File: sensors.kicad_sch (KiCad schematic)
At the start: 9 parts, among them IC7 BME690, U2 BME280, U3 BMP581

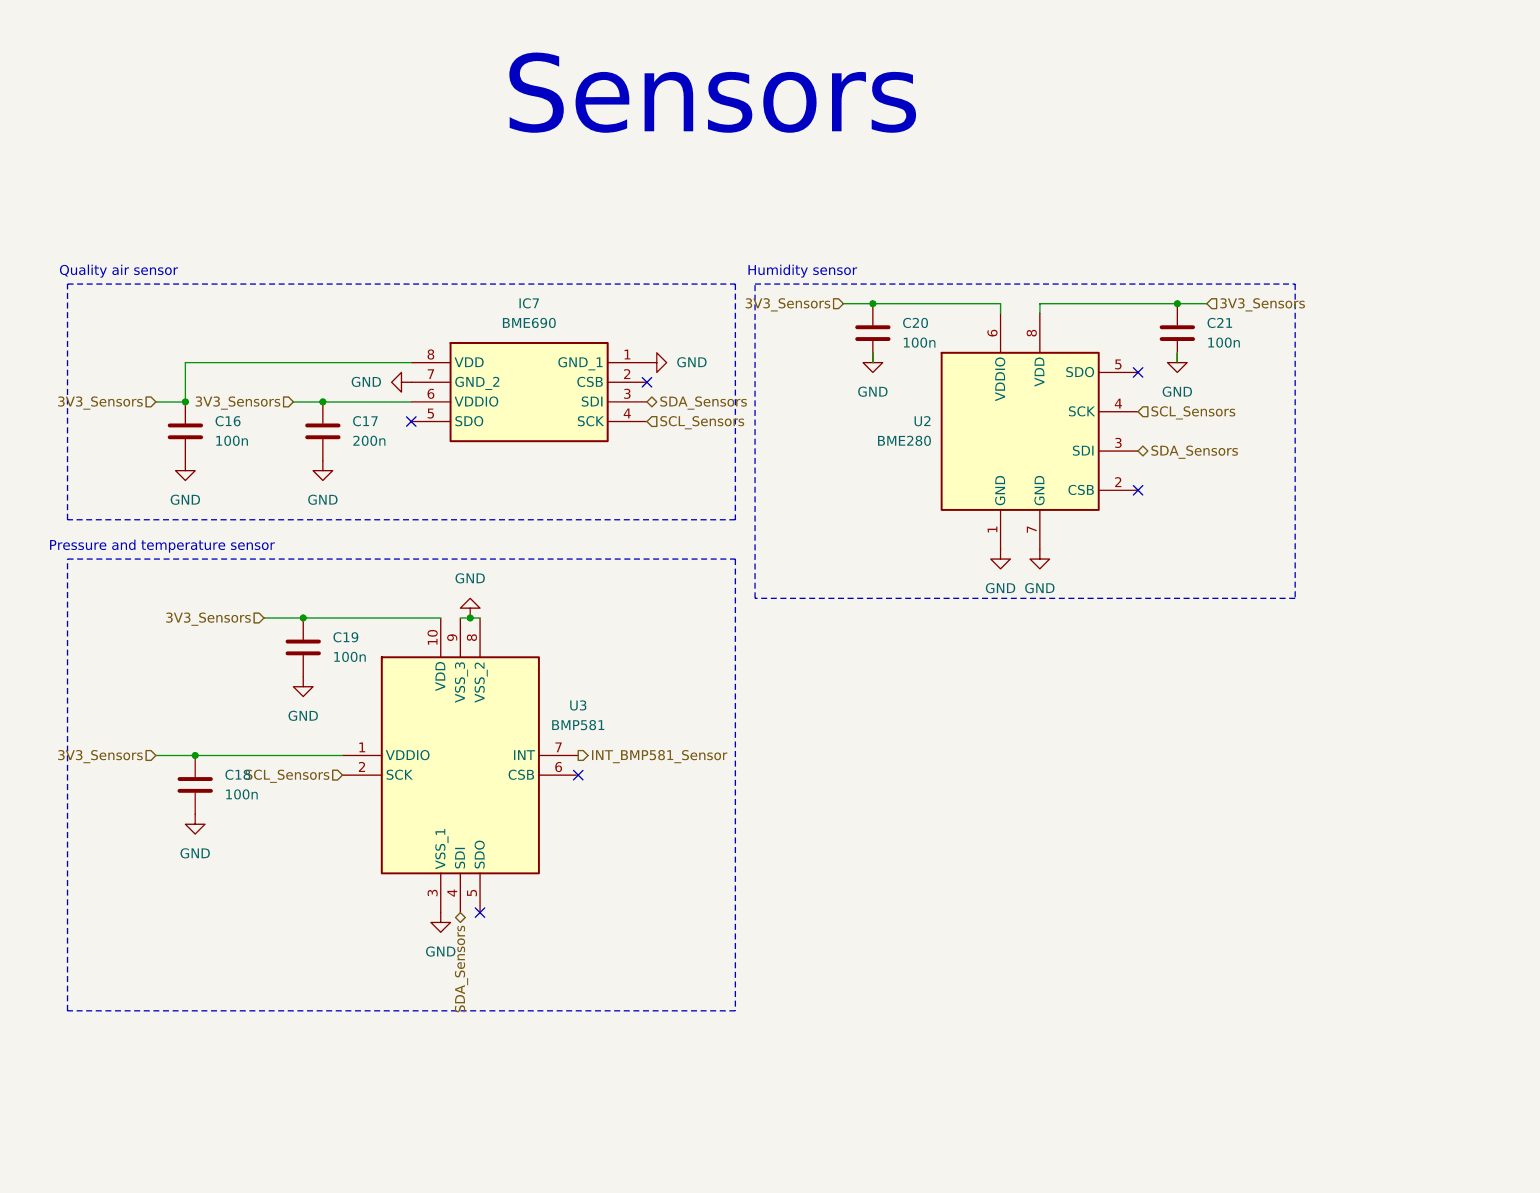
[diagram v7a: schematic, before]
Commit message: Fix some little warnings and refomat schematics files
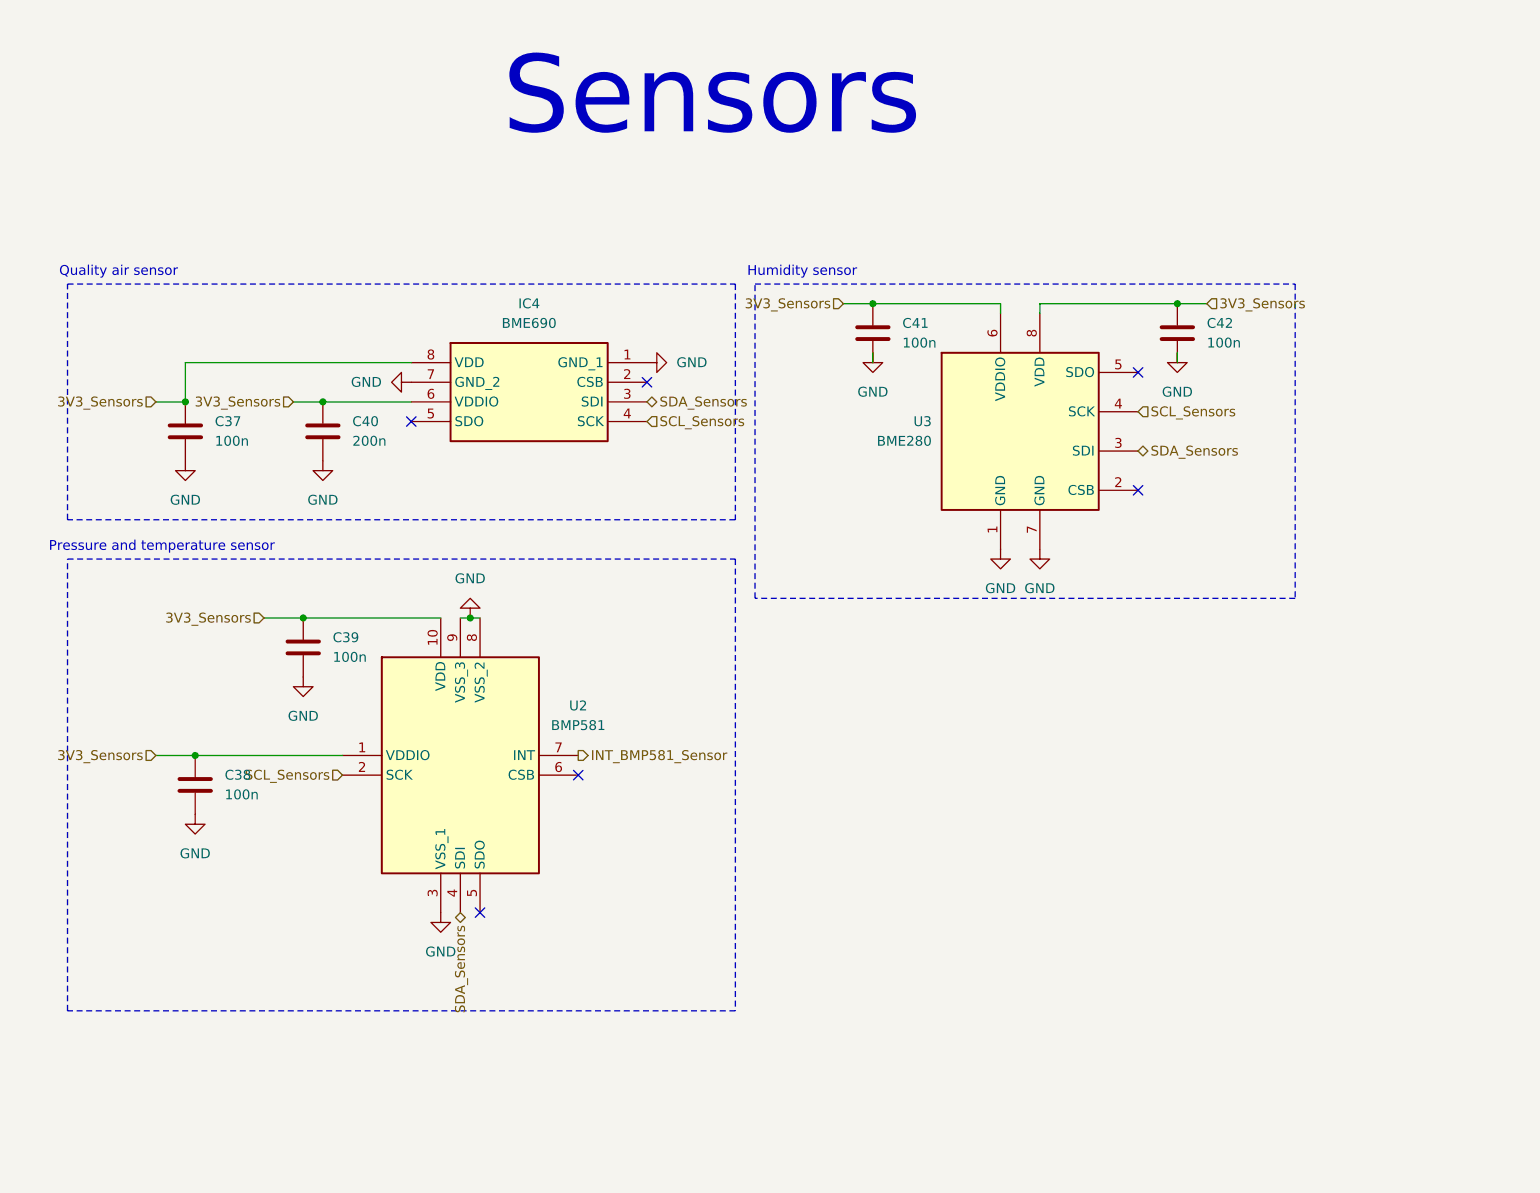
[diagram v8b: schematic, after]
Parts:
- renumbered C16 to C37, C18 to C38, C19 to C39, C17 to C40, C20 to C41, C21 to C42, IC7 to IC4, U3 to U2, U2 to U3
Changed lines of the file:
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@@
 		(dnp no)
 		(fields_autoplaced yes)
-		(property "Reference" "#PWR046"
+		(property "Reference" "#PWR070"
 			(at 170.18 66.04 0)
 			(effects
@@
 			(project "weather-station-poc"
 				(path "/38eb53bb-294e-46e4-ad59-fd355ca373b9/29574217-d56b-4a63-a2c4-128dfec2758e"
-					(reference "#PWR046")
+					(reference "#PWR070")
 					(unit 1)
 				)
@@
 		(dnp no)
 		(fields_autoplaced yes)
-		(property "Reference" "#PWR039"
+		(property "Reference" "#PWR069"
 			(at 147.32 60.96 0)
 			(effects
@@
 			(project "weather-station-poc"
 				(path "/38eb53bb-294e-46e4-ad59-fd355ca373b9/29574217-d56b-4a63-a2c4-128dfec2758e"
-					(reference "#PWR039")
+					(reference "#PWR069")
 					(unit 1)
 				)
@@
 		(dnp no)
 		(fields_autoplaced yes)
-		(property "Reference" "C21"
+		(property "Reference" "C42"
 			(at 213.36 55.8799 0)
 			(effects
@@
 			(project "weather-station-poc"
 				(path "/38eb53bb-294e-46e4-ad59-fd355ca373b9/29574217-d56b-4a63-a2c4-128dfec2758e"
-					(reference "C21")
+					(reference "C42")
 					(unit 1)
 				)
@@
 		(dnp no)
 		(fields_autoplaced yes)
-		(property "Reference" "C16"
+		(property "Reference" "C37"
 			(at 85.09 68.5799 0)
 			(effects
@@
 			(project ""
 				(path "/38eb53bb-294e-46e4-ad59-fd355ca373b9/29574217-d56b-4a63-a2c4-128dfec2758e"
-					(reference "C16")
+					(reference "C37")
 					(unit 1)
 				)
@@
 		(dnp no)
 		(fields_autoplaced yes)
-		(property "Reference" "#PWR036"
+		(property "Reference" "#PWR062"
 			(at 81.28 80.01 0)
 			(effects
@@
 			(project ""
 				(path "/38eb53bb-294e-46e4-ad59-fd355ca373b9/29574217-d56b-4a63-a2c4-128dfec2758e"
-					(reference "#PWR036")
+					(reference "#PWR062")
 					(unit 1)
 				)
@@
 		(dnp no)
 		(fields_autoplaced yes)
-		(property "Reference" "#PWR048"
+		(property "Reference" "#PWR072"
 			(at 191.77 91.44 0)
 			(effects
@@
 			(project "weather-station-poc"
 				(path "/38eb53bb-294e-46e4-ad59-fd355ca373b9/29574217-d56b-4a63-a2c4-128dfec2758e"
-					(reference "#PWR048")
+					(reference "#PWR072")
 					(unit 1)
 				)
@@
 		(dnp no)
 		(fields_autoplaced yes)
-		(property "Reference" "#PWR042"
+		(property "Reference" "#PWR068"
 			(at 118.11 87.63 0)
 			(effects
@@
 			(project "weather-station-poc"
 				(path "/38eb53bb-294e-46e4-ad59-fd355ca373b9/29574217-d56b-4a63-a2c4-128dfec2758e"
-					(reference "#PWR042")
+					(reference "#PWR068")
 					(unit 1)
 				)
@@
 		(dnp no)
 		(fields_autoplaced yes)
-		(property "Reference" "C17"
+		(property "Reference" "C40"
 			(at 102.87 68.5799 0)
 			(effects
@@
 			(project "weather-station-poc"
 				(path "/38eb53bb-294e-46e4-ad59-fd355ca373b9/29574217-d56b-4a63-a2c4-128dfec2758e"
-					(reference "C17")
+					(reference "C40")
 					(unit 1)
 				)
@@
 		(dnp no)
 		(fields_autoplaced yes)
-		(property "Reference" "#PWR037"
+		(property "Reference" "#PWR065"
 			(at 99.06 80.01 0)
 			(effects
@@
 			(project "weather-station-poc"
 				(path "/38eb53bb-294e-46e4-ad59-fd355ca373b9/29574217-d56b-4a63-a2c4-128dfec2758e"
-					(reference "#PWR037")
+					(reference "#PWR065")
 					(unit 1)
 				)
@@
 		(dnp no)
 		(fields_autoplaced yes)
-		(property "Reference" "#PWR045"
+		(property "Reference" "#PWR073"
 			(at 209.55 66.04 0)
 			(effects
@@
 			(project "weather-station-poc"
 				(path "/38eb53bb-294e-46e4-ad59-fd355ca373b9/29574217-d56b-4a63-a2c4-128dfec2758e"
-					(reference "#PWR045")
+					(reference "#PWR073")
 					(unit 1)
 				)
@@
 		(dnp no)
 		(fields_autoplaced yes)
-		(property "Reference" "U3"
+		(property "Reference" "U2"
 			(at 132.08 105.3398 0)
 			(effects
@@
 			(project "weather-station-poc"
 				(path "/38eb53bb-294e-46e4-ad59-fd355ca373b9/29574217-d56b-4a63-a2c4-128dfec2758e"
-					(reference "U3")
+					(reference "U2")
 					(unit 1)
 				)
@@
 		(dnp no)
 		(fields_autoplaced yes)
-		(property "Reference" "#PWR041"
+		(property "Reference" "#PWR063"
 			(at 82.55 125.73 0)
 			(effects
@@
 			(project "weather-station-poc"
 				(path "/38eb53bb-294e-46e4-ad59-fd355ca373b9/29574217-d56b-4a63-a2c4-128dfec2758e"
-					(reference "#PWR041")
+					(reference "#PWR063")
 					(unit 1)
 				)
@@
 		(dnp no)
 		(fields_autoplaced yes)
-		(property "Reference" "#PWR040"
+		(property "Reference" "#PWR064"
 			(at 96.52 107.95 0)
 			(effects
@@
 			(project "weather-station-poc"
 				(path "/38eb53bb-294e-46e4-ad59-fd355ca373b9/29574217-d56b-4a63-a2c4-128dfec2758e"
-					(reference "#PWR040")
+					(reference "#PWR064")
 					(unit 1)
 				)
@@
 		(dnp no)
 		(fields_autoplaced yes)
-		(property "Reference" "U2"
+		(property "Reference" "U3"
 			(at 177.8 68.5799 0)
 			(effects
@@
 			(project "weather-station-poc"
 				(path "/38eb53bb-294e-46e4-ad59-fd355ca373b9/29574217-d56b-4a63-a2c4-128dfec2758e"
-					(reference "U2")
+					(reference "U3")
 					(unit 1)
 				)
@@
 		(dnp no)
 		(fields_autoplaced yes)
-		(property "Reference" "#PWR044"
+		(property "Reference" "#PWR067"
 			(at 114.3 138.43 0)
 			(effects
@@
 			(project "weather-station-poc"
 				(path "/38eb53bb-294e-46e4-ad59-fd355ca373b9/29574217-d56b-4a63-a2c4-128dfec2758e"
-					(reference "#PWR044")
+					(reference "#PWR067")
 					(unit 1)
 				)
@@
 		(dnp no)
 		(fields_autoplaced yes)
-		(property "Reference" "#PWR038"
+		(property "Reference" "#PWR066"
 			(at 104.14 63.5 0)
 			(effects
@@
 			(project "weather-station-poc"
 				(path "/38eb53bb-294e-46e4-ad59-fd355ca373b9/29574217-d56b-4a63-a2c4-128dfec2758e"
-					(reference "#PWR038")
+					(reference "#PWR066")
 					(unit 1)
 				)
@@
 		(dnp no)
 		(fields_autoplaced yes)
-		(property "Reference" "C18"
+		(property "Reference" "C38"
 			(at 86.36 114.2999 0)
 			(effects
@@
 			(project "weather-station-poc"
 				(path "/38eb53bb-294e-46e4-ad59-fd355ca373b9/29574217-d56b-4a63-a2c4-128dfec2758e"
-					(reference "C18")
+					(reference "C38")
 					(unit 1)
 				)
@@
 		(dnp no)
 		(fields_autoplaced yes)
-		(property "Reference" "#PWR047"
+		(property "Reference" "#PWR071"
 			(at 186.69 91.44 0)
 			(effects
@@
 			(project "weather-station-poc"
 				(path "/38eb53bb-294e-46e4-ad59-fd355ca373b9/29574217-d56b-4a63-a2c4-128dfec2758e"
-					(reference "#PWR047")
+					(reference "#PWR071")
 					(unit 1)
 				)
@@
 		(dnp no)
 		(fields_autoplaced yes)
-		(property "Reference" "C19"
+		(property "Reference" "C39"
 			(at 100.33 96.5199 0)
 			(effects
@@
 			(project "weather-station-poc"
 				(path "/38eb53bb-294e-46e4-ad59-fd355ca373b9/29574217-d56b-4a63-a2c4-128dfec2758e"
-					(reference "C19")
+					(reference "C39")
 					(unit 1)
 				)
@@
 		(dnp no)
 		(fields_autoplaced yes)
-		(property "Reference" "C20"
+		(property "Reference" "C41"
 			(at 173.99 55.8799 0)
 			(effects
@@
 			(project "weather-station-poc"
 				(path "/38eb53bb-294e-46e4-ad59-fd355ca373b9/29574217-d56b-4a63-a2c4-128dfec2758e"
-					(reference "C20")
+					(reference "C41")
 					(unit 1)
 				)
@@
 		(dnp no)
 		(fields_autoplaced yes)
-		(property "Reference" "IC7"
+		(property "Reference" "IC4"
 			(at 125.73 53.34 0)
 			(effects
@@
 			(project "weather-station-poc"
 				(path "/38eb53bb-294e-46e4-ad59-fd355ca373b9/29574217-d56b-4a63-a2c4-128dfec2758e"
-					(reference "IC7")
-					(unit 1)
-				)
+					(reference "IC4")
+					(unit 1)
+				)
